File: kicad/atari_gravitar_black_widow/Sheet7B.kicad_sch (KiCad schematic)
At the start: 37 parts, among them Q10 2N3904, Q5 2N3904, Q6 2N3904, Q7 2N3906, Q8 2N3904, Q9 2N3904

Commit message: more cap placements
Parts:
- C118: footprint (none) -> Star_Wars_Vector_PCB:GenericComp
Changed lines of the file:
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@@
       (effects (font (size 1.27 1.27)) (justify left))
     )
-    (property "Footprint" "" (id 2) (at 215.011 307.2638 0)
+    (property "Footprint" "Star_Wars_Vector_PCB:GenericComp" (id 2) (at 215.011 307.2638 0)
       (effects (font (size 1.27 1.27)) hide)
     )

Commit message: caps placement up to c126
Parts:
- C118: footprint Star_Wars_Vector_PCB:GenericComp -> (none)
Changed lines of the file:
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@@
       (effects (font (size 1.27 1.27)) (justify left))
     )
-    (property "Footprint" "Star_Wars_Vector_PCB:GenericComp" (id 2) (at 215.011 307.2638 0)
+    (property "Footprint" "" (id 2) (at 215.011 307.2638 0)
       (effects (font (size 1.27 1.27)) hide)
     )

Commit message: resistor placements R1-R153
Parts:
- R149, R150, R151, R152, R154, R155, R156, R157, R158, R56, R57, R58, R59, R60: footprint (none) -> Star_Wars_Vector_PCB:GenericComp
- R153: footprint (none) -> Star_Wars_Vector_PCB:Inductor1
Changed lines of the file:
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@@
       (effects (font (size 1.27 1.27)) (justify right))
     )
-    (property "Footprint" "" (id 2) (at 467.106 178.181 90)
+    (property "Footprint" "Star_Wars_Vector_PCB:GenericComp" (id 2) (at 467.106 178.181 90)
       (effects (font (size 1.27 1.27)) hide)
     )
@@
     (property "Reference" "R58" (id 0) (at 184.023 241.173 90))
     (property "Value" "4.7k" (id 1) (at 184.15 237.1876 90))
-    (property "Footprint" "" (id 2) (at 183.896 240.284 90)
+    (property "Footprint" "Star_Wars_Vector_PCB:GenericComp" (id 2) (at 183.896 240.284 90)
       (effects (font (size 1.27 1.27)) hide)
     )
@@
       (effects (font (size 1.27 1.27)) (justify right))
     )
-    (property "Footprint" "" (id 2) (at 423.291 245.364 90)
+    (property "Footprint" "Star_Wars_Vector_PCB:GenericComp" (id 2) (at 423.291 245.364 90)
       (effects (font (size 1.27 1.27)) hide)
     )
@@
     (property "Reference" "R150" (id 0) (at 209.677 290.2925 90))
     (property "Value" "22k" (id 1) (at 209.677 293.0676 90))
-    (property "Footprint" "" (id 2) (at 209.423 296.164 90)
+    (property "Footprint" "Star_Wars_Vector_PCB:GenericComp" (id 2) (at 209.423 296.164 90)
       (effects (font (size 1.27 1.27)) hide)
     )
@@
     (property "Reference" "R153" (id 0) (at 219.329 277.0845 90))
     (property "Value" "68" (id 1) (at 219.329 279.8596 90))
-    (property "Footprint" "" (id 2) (at 219.583 280.924 90)
+    (property "Footprint" "Star_Wars_Vector_PCB:Inductor1" (id 2) (at 219.583 280.924 90)
       (effects (font (size 1.27 1.27)) hide)
     )
@@
       (effects (font (size 1.27 1.27)) (justify right))
     )
-    (property "Footprint" "" (id 2) (at 396.24 245.364 90)
+    (property "Footprint" "Star_Wars_Vector_PCB:GenericComp" (id 2) (at 396.24 245.364 90)
       (effects (font (size 1.27 1.27)) hide)
     )
@@
     (property "Reference" "R57" (id 0) (at 184.15 230.759 90))
     (property "Value" "4.7k" (id 1) (at 184.15 227.076 90))
-    (property "Footprint" "" (id 2) (at 183.896 230.124 90)
+    (property "Footprint" "Star_Wars_Vector_PCB:GenericComp" (id 2) (at 183.896 230.124 90)
       (effects (font (size 1.27 1.27)) hide)
     )
@@
       (effects (font (size 1.27 1.27)) (justify right))
     )
-    (property "Footprint" "" (id 2) (at 229.743 249.809 90)
+    (property "Footprint" "Star_Wars_Vector_PCB:GenericComp" (id 2) (at 229.743 249.809 90)
       (effects (font (size 1.27 1.27)) hide)
     )
@@
       (effects (font (size 1.27 1.27)) (justify right))
     )
-    (property "Footprint" "" (id 2) (at 186.944 254.762 90)
+    (property "Footprint" "Star_Wars_Vector_PCB:GenericComp" (id 2) (at 186.944 254.762 90)
       (effects (font (size 1.27 1.27)) hide)
     )
@@
       (effects (font (size 1.27 1.27)) (justify left))
     )
-    (property "Footprint" "" (id 2) (at 188.976 208.534 90)
+    (property "Footprint" "Star_Wars_Vector_PCB:GenericComp" (id 2) (at 188.976 208.534 90)
       (effects (font (size 1.27 1.27)) hide)
     )
@@
       (effects (font (size 1.27 1.27)) (justify right))
     )
-    (property "Footprint" "" (id 2) (at 406.146 178.181 90)
+    (property "Footprint" "Star_Wars_Vector_PCB:GenericComp" (id 2) (at 406.146 178.181 90)
       (effects (font (size 1.27 1.27)) hide)
     )
@@
     (property "Reference" "R56" (id 0) (at 184.023 236.093 90))
     (property "Value" "4.7k" (id 1) (at 184.15 232.1076 90))
-    (property "Footprint" "" (id 2) (at 183.896 235.204 90)
+    (property "Footprint" "Star_Wars_Vector_PCB:GenericComp" (id 2) (at 183.896 235.204 90)
       (effects (font (size 1.27 1.27)) hide)
     )
@@
       (effects (font (size 1.27 1.27)) (justify left))
     )
-    (property "Footprint" "" (id 2) (at 183.896 225.044 90)
+    (property "Footprint" "Star_Wars_Vector_PCB:GenericComp" (id 2) (at 183.896 225.044 90)
       (effects (font (size 1.27 1.27)) hide)
     )
@@
       (effects (font (size 1.27 1.27)) (justify right))
     )
-    (property "Footprint" "" (id 2) (at 433.197 178.181 90)
+    (property "Footprint" "Star_Wars_Vector_PCB:GenericComp" (id 2) (at 433.197 178.181 90)
       (effects (font (size 1.27 1.27)) hide)
     )
@@
       (effects (font (size 1.27 1.27)) (justify right))
     )
-    (property "Footprint" "" (id 2) (at 457.2 245.491 90)
-      (effects (font (size 1.27 1.27)) hide)
-    )
+    (property "Footprint" "Star_Wars_Vector_PCB:GenericComp" (id 2) (at 457.2 245.491 90)
+      (effects (font (size 1.27 1.27)) hide)
+    )

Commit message: ALL PARTS PLACED!!
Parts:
- C118: footprint (none) -> Star_Wars_Vector_PCB:CapBrown
- Q10, Q5, Q6, Q7, Q8, Q9: footprint (none) -> quantum_arcade_pcb:GenTrans
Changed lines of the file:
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@@
       (effects (font (size 1.27 1.27)) (justify left))
     )
-    (property "Footprint" "" (id 2) (at 225.679 297.053 0)
+    (property "Footprint" "quantum_arcade_pcb:GenTrans" (id 2) (at 225.679 297.053 0)
       (effects (font (size 1.27 1.27) italic) (justify left) hide)
     )
@@
     (property "Reference" "Q6" (id 0) (at 397.256 169.1091 90))
     (property "Value" "2N3904" (id 1) (at 397.256 171.8842 90))
-    (property "Footprint" "" (id 2) (at 399.161 172.085 0)
+    (property "Footprint" "quantum_arcade_pcb:GenTrans" (id 2) (at 399.161 172.085 0)
       (effects (font (size 1.27 1.27) italic) (justify left) hide)
     )
@@
     (property "Reference" "Q10" (id 0) (at 458.216 169.1091 90))
     (property "Value" "2N3904" (id 1) (at 458.216 171.8842 90))
-    (property "Footprint" "" (id 2) (at 460.121 172.085 0)
+    (property "Footprint" "quantum_arcade_pcb:GenTrans" (id 2) (at 460.121 172.085 0)
       (effects (font (size 1.27 1.27) italic) (justify left) hide)
     )
@@
       (effects (font (size 1.27 1.27)) (justify left))
     )
-    (property "Footprint" "" (id 2) (at 215.011 307.2638 0)
+    (property "Footprint" "Star_Wars_Vector_PCB:CapBrown" (id 2) (at 215.011 307.2638 0)
       (effects (font (size 1.27 1.27)) hide)
     )
@@
       (effects (font (size 1.27 1.27)) (justify left))
     )
-    (property "Footprint" "" (id 2) (at 233.299 243.078 0)
+    (property "Footprint" "quantum_arcade_pcb:GenTrans" (id 2) (at 233.299 243.078 0)
       (effects (font (size 1.27 1.27) italic) (justify left) hide)
     )
@@
       (effects (font (size 1.27 1.27)) (justify left))
     )
-    (property "Footprint" "" (id 2) (at 214.249 251.206 0)
+    (property "Footprint" "quantum_arcade_pcb:GenTrans" (id 2) (at 214.249 251.206 0)
       (effects (font (size 1.27 1.27) italic) (justify left) hide)
     )
@@
     (property "Reference" "Q8" (id 0) (at 424.307 169.1091 90))
     (property "Value" "2N3904" (id 1) (at 424.307 171.8842 90))
-    (property "Footprint" "" (id 2) (at 426.212 172.085 0)
+    (property "Footprint" "quantum_arcade_pcb:GenTrans" (id 2) (at 426.212 172.085 0)
       (effects (font (size 1.27 1.27) italic) (justify left) hide)
     )

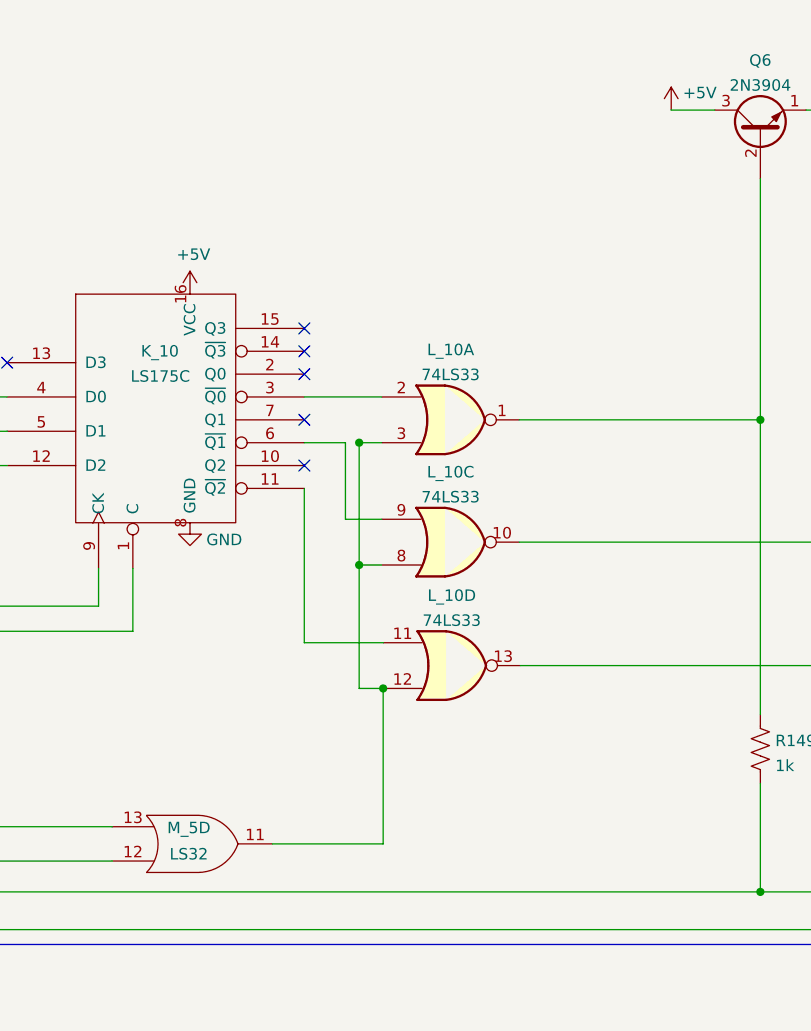
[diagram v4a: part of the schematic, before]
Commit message: Fixed all schematic warnings and fixed the edge cuts
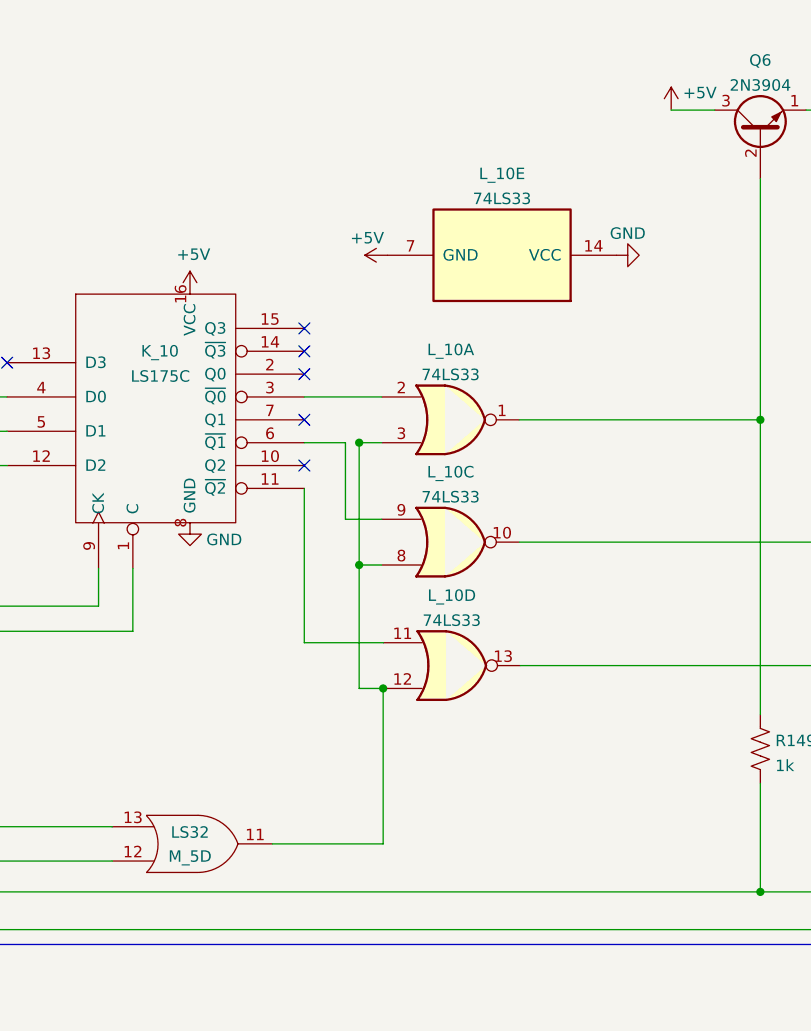
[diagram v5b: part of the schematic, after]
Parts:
- removed M_5: LS32, Star_Wars_Vector_PCB:DIP14, symbol atari_grav_bw:LS32
- added unit 5 of L_10
- added M_5: LS32, Star_Wars_Vector_PCB:DIP14, symbol Star_Wars_Vector_PCB:LS32
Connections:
- net +5V: now also L_10.7 (GND)
- net GND: now also L_10.14 (VCC)
- net at L_10.12, L_10.3, L_10.8: now also M_5.11
- net at C118.1, N_5.13, R150.2: now also M_5.13
- net at J_3.2: now also M_5.12
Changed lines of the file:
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@@
+    (pin "1")
+  )
+  (symbol (lib_id "power:+5V") (at 355.854 190.754 90) (unit 1)
+    (in_bom yes) (on_board yes)
+    (property "Reference" "#PWR0549" (id 0) (at 359.664 190.754 0)
+      (effects (font (size 1.27 1.27)) hide)
+    )
+    (property "Value" "+5V" (id 1) (at 353.568 188.849 90))
+    (property "Footprint" "" (id 2) (at 355.854 190.754 0)
+      (effects (font (size 1.27 1.27)) hide)
+    )
+    (property "Datasheet" "" (id 3) (at 355.854 190.754 0)
+      (effects (font (size 1.27 1.27)) hide)
+    )
     (pin "1")
   )
@@
     (pin "1")
   )
+  (symbol (lib_id "power:GND") (at 381.254 190.754 90) (unit 1)
+    (in_bom yes) (on_board yes)
+    (property "Reference" "#PWR0550" (id 0) (at 387.604 190.754 0)
+      (effects (font (size 1.27 1.27)) hide)
+    )
+    (property "Value" "GND" (id 1) (at 382.524 188.341 90))
+    (property "Footprint" "" (id 2) (at 381.254 190.754 0)
+      (effects (font (size 1.27 1.27)) hide)
+    )
+    (property "Datasheet" "" (id 3) (at 381.254 190.754 0)
+      (effects (font (size 1.27 1.27)) hide)
+    )
+    (pin "1")
+  )
   (symbol (lib_id "power:GND") (at 150.368 319.405 0) (unit 1)
     (in_bom yes) (on_board yes)
@@
     (pin "9")
   )
+  (symbol (lib_id "74xx:74LS33") (at 368.554 190.754 270) (mirror x) (unit 5)
+    (in_bom yes) (on_board yes) (fields_autoplaced)
+    (property "Reference" "L_10" (id 0) (at 368.554 181.7075 90))
+    (property "Value" "74LS33" (id 1) (at 368.554 184.4826 90))
+    (property "Footprint" "Star_Wars_Vector_PCB:DIP14" (id 2) (at 368.554 190.754 0)
+      (effects (font (size 1.27 1.27)) hide)
+    )
+    (property "Datasheet" "http://www.ti.com/lit/gpn/sn74LS33" (id 3) (at 368.554 190.754 0)
+      (effects (font (size 1.27 1.27)) hide)
+    )
+    (pin "14")
+    (pin "7")
+  )
   (symbol (lib_id "power:+5V") (at 215.519 281.94 90) (unit 1)
     (in_bom yes) (on_board yes)
@@
     (pin "3")
   )
-  (symbol (lib_id "power:GND") (at 128.143 247.523 0) (unit 1)
-    (in_bom yes) (on_board yes)
-    (property "Reference" "#PWR0343" (id 0) (at 128.143 253.873 0)
-      (effects (font (size 1.27 1.27)) hide)
-    )
-    (property "Value" "GND" (id 1) (at 131.953 249.428 0))
-    (property "Footprint" "" (id 2) (at 128.143 247.523 0)
-      (effects (font (size 1.27 1.27)) hide)
-    )
-    (property "Datasheet" "" (id 3) (at 128.143 247.523 0)
-      (effects (font (size 1.27 1.27)) hide)
-    )
-    (pin "1")
-  )
-  (symbol (lib_id "power:+5V") (at 333.883 195.072 0) (unit 1)
-    (in_bom yes) (on_board yes)
-    (property "Reference" "#PWR0334" (id 0) (at 333.883 198.882 0)
-      (effects (font (size 1.27 1.27)) hide)
-    )
-    (property "Value" "+5V" (id 1) (at 334.264 190.6778 0))
-    (property "Footprint" "" (id 2) (at 333.883 195.072 0)
-      (effects (font (size 1.27 1.27)) hide)
-    )
-    (property "Datasheet" "" (id 3) (at 333.883 195.072 0)
-      (effects (font (size 1.27 1.27)) hide)
-    )
-    (pin "1")
-  )
-  (symbol (lib_id "atari_grav_bw:LS32") (at 334.137 256.159 0) (mirror x) (unit 4)
-    (in_bom yes) (on_board yes)
-    (property "Reference" "M_5" (id 0) (at 333.756 254.381 0))
-    (property "Value" "LS32" (id 1) (at 333.756 257.302 0))
+  (symbol (lib_id "Star_Wars_Vector_PCB:LS32") (at 334.137 256.159 0) (mirror x) (unit 4)
+    (in_bom yes) (on_board yes)
+    (property "Reference" "M_5" (id 0) (at 333.883 257.556 0))
+    (property "Value" "LS32" (id 1) (at 333.883 254.889 0))
     (property "Footprint" "Star_Wars_Vector_PCB:DIP14" (id 2) (at 334.137 256.159 0)
       (effects (font (size 1.27 1.27)) hide)
@@
     (pin "13")
   )
+  (symbol (lib_id "power:GND") (at 128.143 247.523 0) (unit 1)
+    (in_bom yes) (on_board yes)
+    (property "Reference" "#PWR0343" (id 0) (at 128.143 253.873 0)
+      (effects (font (size 1.27 1.27)) hide)
+    )
+    (property "Value" "GND" (id 1) (at 131.953 249.428 0))
+    (property "Footprint" "" (id 2) (at 128.143 247.523 0)
+      (effects (font (size 1.27 1.27)) hide)
+    )
+    (property "Datasheet" "" (id 3) (at 128.143 247.523 0)
+      (effects (font (size 1.27 1.27)) hide)
+    )
+    (pin "1")
+  )
+  (symbol (lib_id "power:+5V") (at 333.883 195.072 0) (unit 1)
+    (in_bom yes) (on_board yes)
+    (property "Reference" "#PWR0334" (id 0) (at 333.883 198.882 0)
+      (effects (font (size 1.27 1.27)) hide)
+    )
+    (property "Value" "+5V" (id 1) (at 334.264 190.6778 0))
+    (property "Footprint" "" (id 2) (at 333.883 195.072 0)
+      (effects (font (size 1.27 1.27)) hide)
+    )
+    (property "Datasheet" "" (id 3) (at 333.883 195.072 0)
+      (effects (font (size 1.27 1.27)) hide)
+    )
+    (pin "1")
+  )
   (symbol (lib_id "atari_gravitar_black_widow-rescue:2N3906-Star_Wars_Vector_PCB-rescue") (at 209.169 249.301 0) (unit 1)

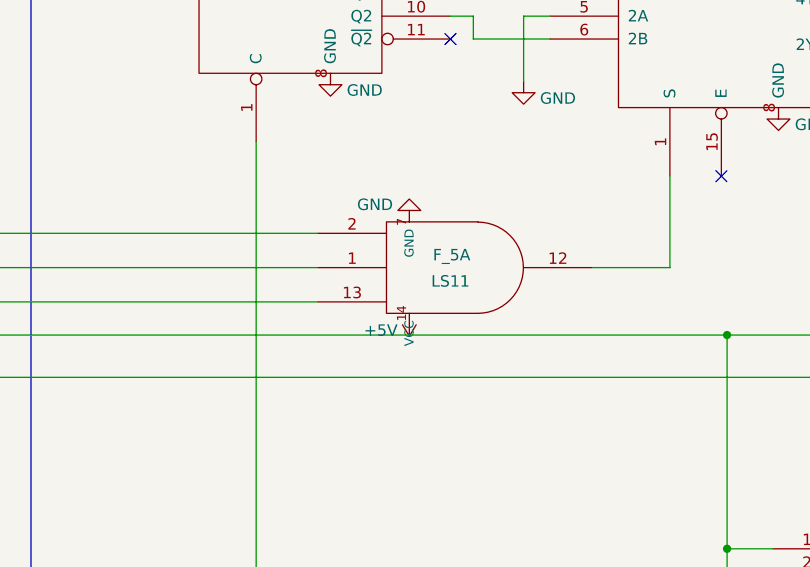
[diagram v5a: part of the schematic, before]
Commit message: Fixed all warning on PCB layout
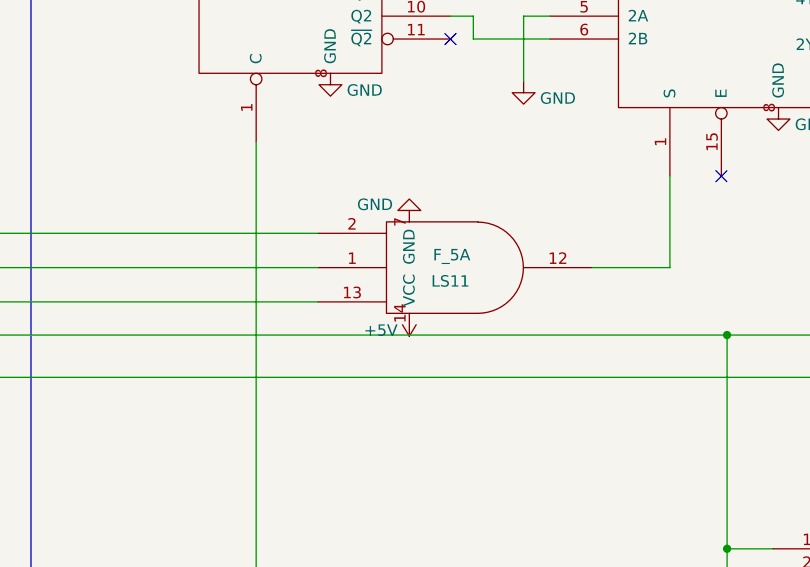
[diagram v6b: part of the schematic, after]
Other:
- moved on the sheet: F_5A
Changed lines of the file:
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@@
       (effects (font (size 1.27 1.27)) hide)
     )
-    (pin "14")
-    (pin "7")
     (pin "1")
     (pin "12")
     (pin "13")
+    (pin "14")
     (pin "2")
+    (pin "7")
   )
   (symbol (lib_id "power:GND") (at 87.122 260.223 180) (unit 1)

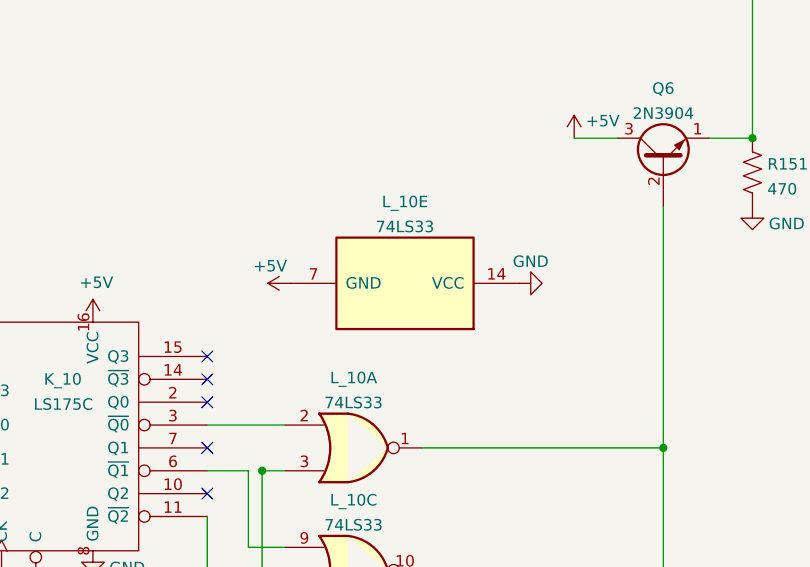
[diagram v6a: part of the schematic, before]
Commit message: more top traces completed
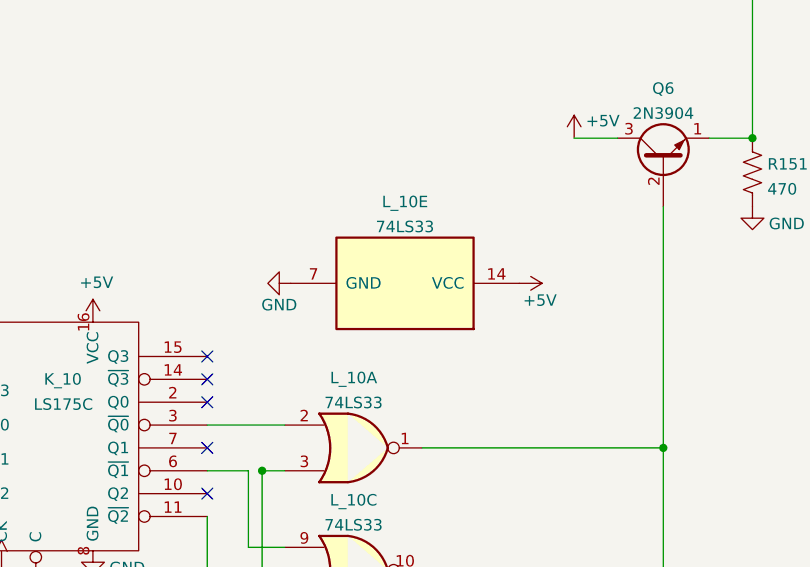
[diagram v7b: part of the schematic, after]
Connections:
- net +5V: now also L_10.14 (VCC); no longer L_10.7 (GND)
- net GND: now also L_10.7 (GND); no longer L_10.14 (VCC)
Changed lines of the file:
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@@
     (pin "1")
   )
-  (symbol (lib_id "power:+5V") (at 355.854 190.754 90) (unit 1)
-    (in_bom yes) (on_board yes)
-    (property "Reference" "#PWR0549" (id 0) (at 359.664 190.754 0)
-      (effects (font (size 1.27 1.27)) hide)
-    )
-    (property "Value" "+5V" (id 1) (at 353.568 188.849 90))
-    (property "Footprint" "" (id 2) (at 355.854 190.754 0)
-      (effects (font (size 1.27 1.27)) hide)
-    )
-    (property "Datasheet" "" (id 3) (at 355.854 190.754 0)
+  (symbol (lib_id "power:+5V") (at 381.254 190.754 270) (unit 1)
+    (in_bom yes) (on_board yes)
+    (property "Reference" "#PWR0549" (id 0) (at 377.444 190.754 0)
+      (effects (font (size 1.27 1.27)) hide)
+    )
+    (property "Value" "+5V" (id 1) (at 383.54 192.659 90))
+    (property "Footprint" "" (id 2) (at 381.254 190.754 0)
+      (effects (font (size 1.27 1.27)) hide)
+    )
+    (property "Datasheet" "" (id 3) (at 381.254 190.754 0)
       (effects (font (size 1.27 1.27)) hide)
     )
@@
     (pin "1")
   )
-  (symbol (lib_id "power:GND") (at 381.254 190.754 90) (unit 1)
-    (in_bom yes) (on_board yes)
-    (property "Reference" "#PWR0550" (id 0) (at 387.604 190.754 0)
-      (effects (font (size 1.27 1.27)) hide)
-    )
-    (property "Value" "GND" (id 1) (at 382.524 188.341 90))
-    (property "Footprint" "" (id 2) (at 381.254 190.754 0)
-      (effects (font (size 1.27 1.27)) hide)
-    )
-    (property "Datasheet" "" (id 3) (at 381.254 190.754 0)
-      (effects (font (size 1.27 1.27)) hide)
-    )
+  (symbol (lib_id "power:GND") (at 355.854 190.754 270) (unit 1)
+    (in_bom yes) (on_board yes)
+    (property "Reference" "#PWR0550" (id 0) (at 349.504 190.754 0)
+      (effects (font (size 1.27 1.27)) hide)
+    )
+    (property "Value" "GND" (id 1) (at 354.584 193.167 90))
+    (property "Footprint" "" (id 2) (at 355.854 190.754 0)
+      (effects (font (size 1.27 1.27)) hide)
+    )
+    (property "Datasheet" "" (id 3) (at 355.854 190.754 0)
+      (effects (font (size 1.27 1.27)) hide)
+    )
